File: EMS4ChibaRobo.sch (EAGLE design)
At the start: 31 parts, among them CON1 XT60PB-F, CON2 XT60PB-M, CON3 XT60PB-M, Q2 BUZ11BH, U1 V23134J1052D642, U10 MC34063AD, U4 TLP184, U9 XC6206

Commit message: 大幅な設計変更
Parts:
- removed C22: 47u, rcl:CPOL-EUE2.5-5
- removed C5, C7: 100n, rcl:C-EUC0603
- removed C6: 100p, rcl:C-EUC0603
- removed D3: PMEG6010CEJ,115, nexperia:PMEG6010CEJ,115
- removed L1: L5852, inductors:L5852
- removed R11: 0.68, rcl:R-EU_R1206
- removed R18: 3.6k, rcl:R-EU_R0603
- removed R19: 1.2k, rcl:R-EU_R0603
- removed R28, R30: 1k, rcl:R-EU_R0603
- removed U10: MC34063AD, mc34063:MC34063AD
- removed U4: TLP184, md201x:TLP184
- added C1: 22u, rcl:CPOL-EUE2.5-5
- added C2: 100n, rcl:C-EUC0603
- added IC1: 7805DT, linear:7805DT
- added U$3, U$4: XH-2-STRAIGHT, con-xh:XH-2-STRAIGHT
- renumbered Q2 to Q1
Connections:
- removed net N$1: R11.2, U10.DC, U10.IS, U10.SWC
- removed net N$26: D3.C, L1.1, U10.SWE
- removed net N$27: C6.1, U10.TC
- removed net N$28: R18.1, R19.2, U10.FB
- removed net N$30: R28.1, U4.AC1
- removed net SEND_EMS: U$1.2, U$2.1
- new net LOG_OUT: F1.1, U$3.2, U$4.2
- net !EMS: now also U$1.1; no longer R30.2, U4.E
- net !EMS_ISO: no longer R28.2
- net +12V: now also C1.+, IC1.VI; no longer C7.1, R11.1, U10.VCC
- net +3V3: now also U$1.2; no longer U4.C
- net +5V: now also C2.1, IC1.VO; no longer C22.+, C5.1, L1.2, R18.2, U$1.1
- net BATT_POWER: no longer F1.1
- net GNDIO: now also C1.-, C2.2, IC1.GND, U$2.1, U$3.1, U$4.1; no longer C22.-, C5.2, C6.2, C7.2, D3.A, R19.1, R30.1, U10.GND, U4.AC2
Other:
- moved on the sheet: C19, C20, U9

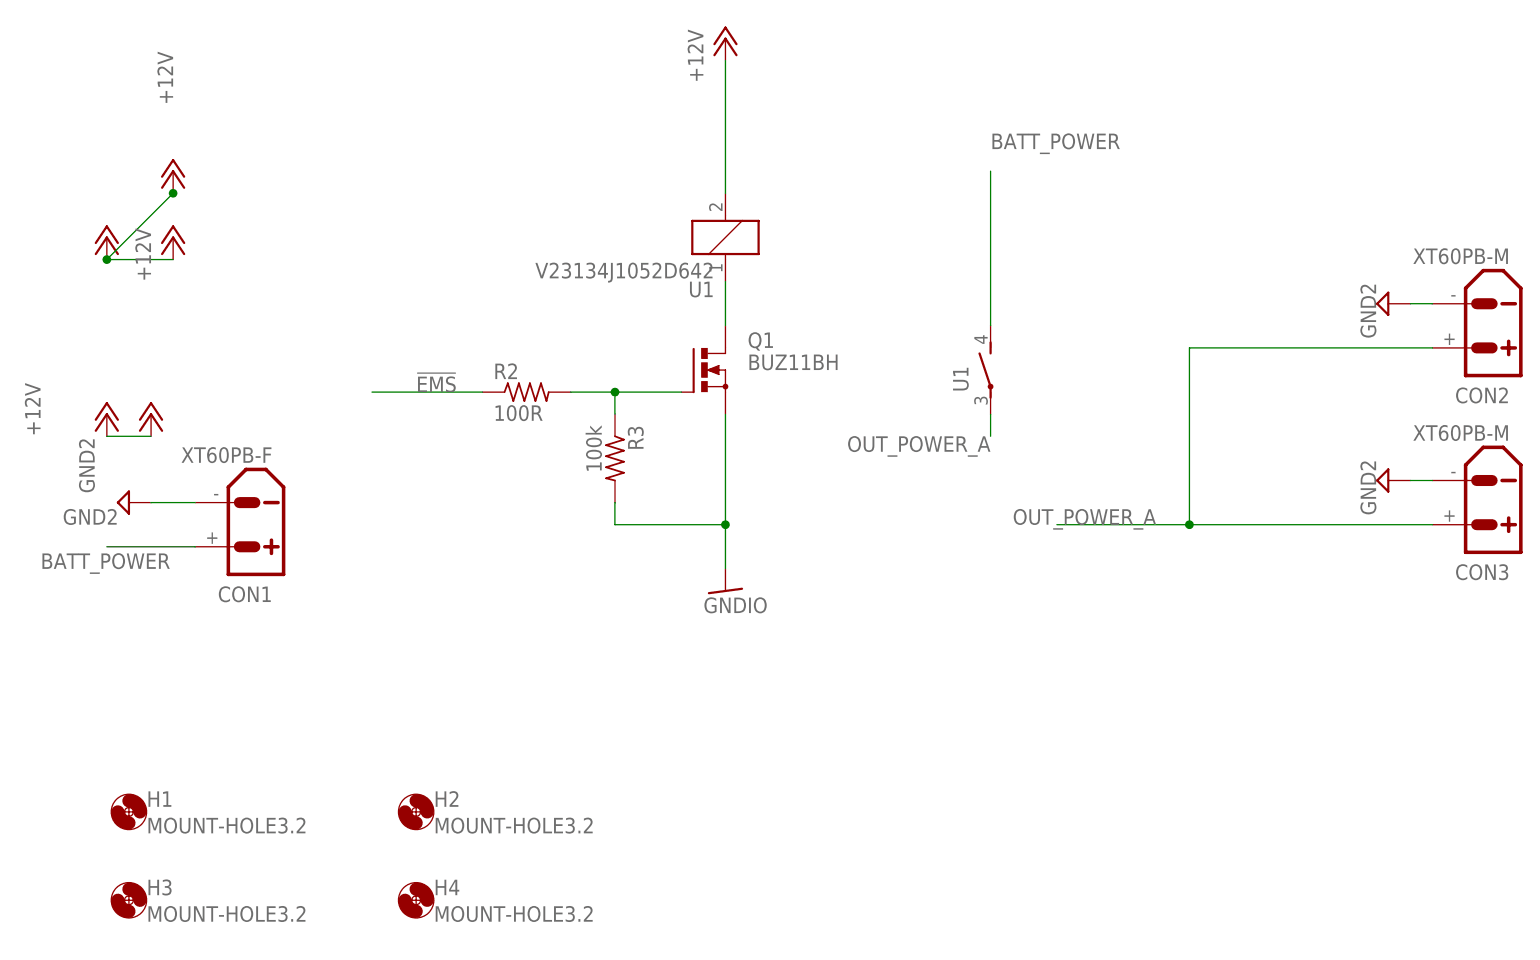
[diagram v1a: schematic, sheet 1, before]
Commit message: relayのフットプリントの改善
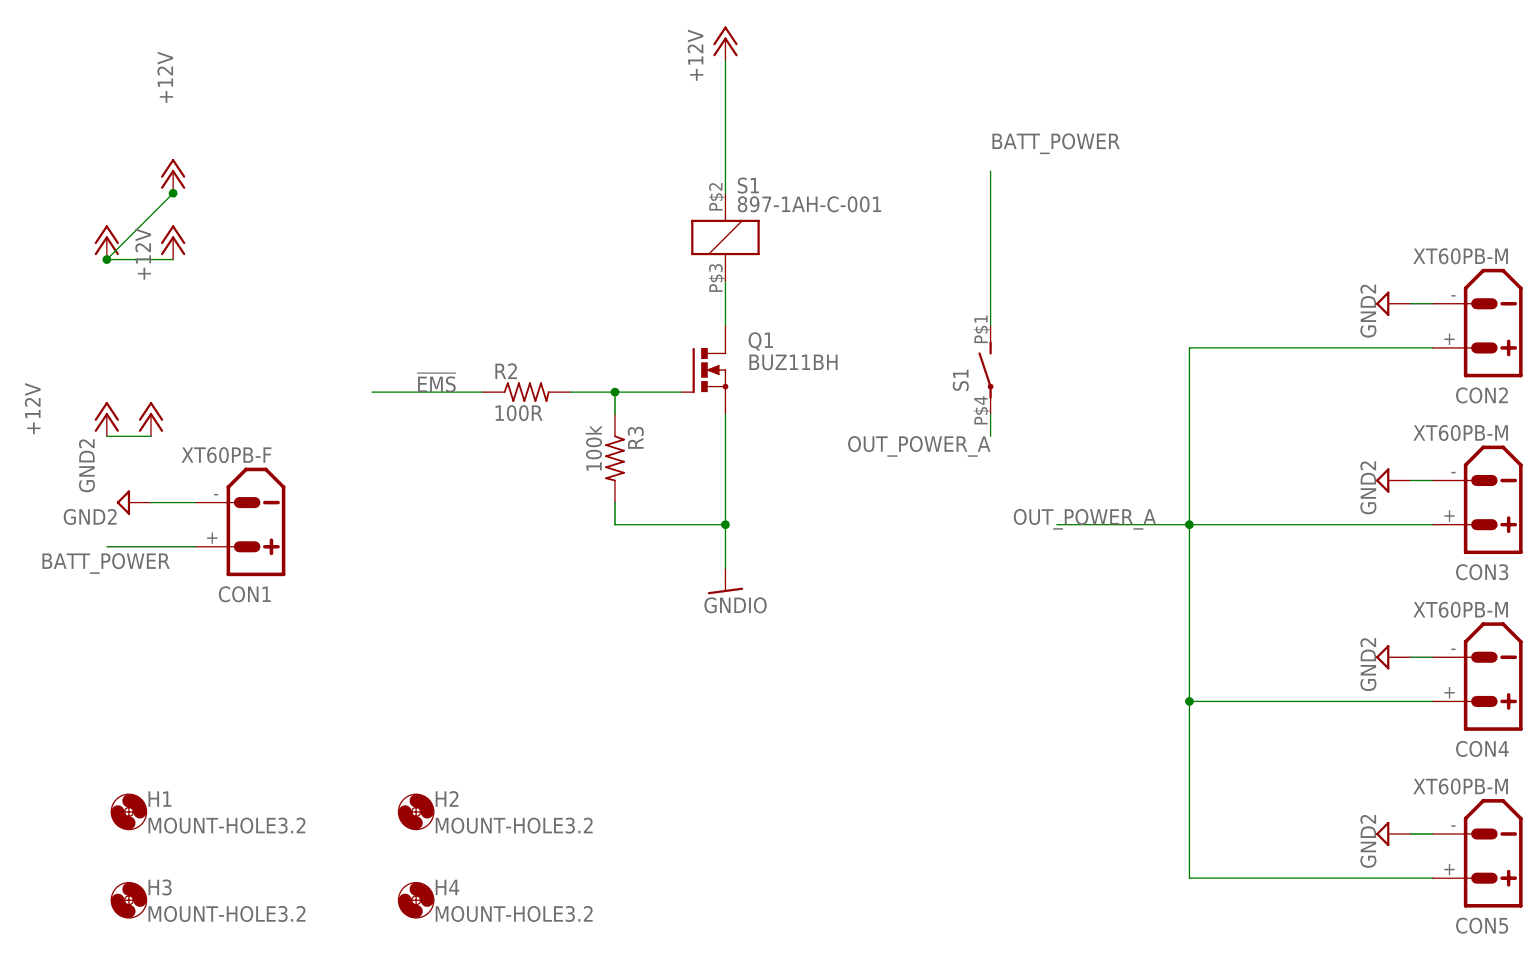
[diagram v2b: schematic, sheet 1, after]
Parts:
- removed U1: V23134J1052D642, relay:V23134J1052D642
- added CON4, CON5: XT60PB-M, amass:XT60PB-M
- added S1: 897-1AH-C-001, relay:897-1AH-C-001
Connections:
- removed net !EMS_ISO: U$2.2
- removed net N$6: Q1.D, U1A.1
- new net N$1: Q1.D, S1U1.2
- net !EMS: now also U$2.2
- net +12V: now also S1U1.1; no longer U1A.2
- net BATT_POWER: now also S1U2.S; no longer U1B.S
- net GND2: now also CON4.-, CON5.-
- net OUT_POWER_A: now also CON4.+, CON5.+, S1U2.P; no longer U1B.P
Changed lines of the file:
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@@
 <part name="SUPPLY7" library="supply2" library_urn="urn:adsk.eagle:library:372" deviceset="GND2" device=""/>
 <part name="SUPPLY8" library="supply2" library_urn="urn:adsk.eagle:library:372" deviceset="GND2" device=""/>
-<part name="U1" library="relay" deviceset="V23134J1052D642" device=""/>
 <part name="H1" library="holes" library_urn="urn:adsk.eagle:library:237" deviceset="MOUNT-HOLE" device="3.2" package3d_urn="urn:adsk.eagle:package:14275/1"/>
 <part name="H2" library="holes" library_urn="urn:adsk.eagle:library:237" deviceset="MOUNT-HOLE" device="3.2" package3d_urn="urn:adsk.eagle:package:14275/1"/>
@@
 <part name="C1" library="rcl" library_urn="urn:adsk.eagle:library:334" deviceset="CPOL-EU" device="E2.5-5" package3d_urn="urn:adsk.eagle:package:23344/1" value="22u"/>
 <part name="C2" library="rcl" library_urn="urn:adsk.eagle:library:334" deviceset="C-EU" device="C0603" package3d_urn="urn:adsk.eagle:package:23616/2" value="100n"/>
+<part name="SUPPLY2" library="supply2" library_urn="urn:adsk.eagle:library:372" deviceset="GND2" device=""/>
+<part name="SUPPLY3" library="supply2" library_urn="urn:adsk.eagle:library:372" deviceset="GND2" device=""/>
+<part name="CON4" library="amass" deviceset="XT60" device="PB-M"/>
+<part name="CON5" library="amass" deviceset="XT60" device="PB-M"/>
+<part name="S1" library="relay" deviceset="897-1AH-C-001" device=""/>
 </parts>
 <sheets>
@@
 <attribute name="VALUE" x="146.685" y="58.293" size="1.778" layer="96" rot="R270"/>
 </instance>
-<instance part="U1" gate="A" x="73.66" y="83.82" smashed="yes" rot="R180">
-<attribute name="VALUE" x="72.39" y="80.899" size="1.778" layer="96" rot="R180"/>
-<attribute name="PART" x="72.39" y="78.74" size="1.778" layer="95" rot="R180"/>
-</instance>
-<instance part="U1" gate="B" x="104.14" y="68.58" smashed="yes">
-<attribute name="PART" x="101.6" y="66.04" size="1.778" layer="95" rot="R90"/>
-</instance>
 <instance part="H1" gate="G$1" x="5.08" y="17.78" smashed="yes">
 <attribute name="NAME" x="7.112" y="18.3642" size="1.778" layer="95"/>
@@
 <attribute name="NAME" x="76.2" y="71.12" size="1.778" layer="95"/>
 <attribute name="VALUE" x="76.2" y="68.58" size="1.778" layer="96"/>
+</instance>
+<instance part="SUPPLY2" gate="G$1" x="149.86" y="15.24" smashed="yes" rot="R270">
+<attribute name="VALUE" x="146.685" y="17.653" size="1.778" layer="96" rot="R270"/>
+</instance>
+<instance part="SUPPLY3" gate="G$1" x="149.86" y="35.56" smashed="yes" rot="R270">
+<attribute name="VALUE" x="146.685" y="37.973" size="1.778" layer="96" rot="R270"/>
+</instance>
+<instance part="CON4" gate="G$1" x="160.02" y="33.02" smashed="yes" rot="R180">
+<attribute name="VALUE" x="163.83" y="41.91" size="1.778" layer="96" rot="R180"/>
+<attribute name="NAME" x="163.83" y="25.908" size="1.778" layer="95" rot="R180"/>
+</instance>
+<instance part="CON5" gate="G$1" x="160.02" y="12.7" smashed="yes" rot="R180">
+<attribute name="VALUE" x="163.83" y="21.59" size="1.778" layer="96" rot="R180"/>
+<attribute name="NAME" x="163.83" y="5.588" size="1.778" layer="95" rot="R180"/>
+</instance>
+<instance part="S1" gate="U1" x="73.66" y="83.82" smashed="yes">
+<attribute name="VALUE" x="74.93" y="86.741" size="1.778" layer="96"/>
+<attribute name="PART" x="74.93" y="88.9" size="1.778" layer="95"/>
+</instance>
+<instance part="S1" gate="U2" x="104.14" y="68.58" smashed="yes">
+<attribute name="PART" x="101.6" y="66.04" size="1.778" layer="95" rot="R90"/>
 </instance>
 </instances>
@@
 <wire x1="154.94" y1="55.88" x2="152.4" y2="55.88" width="0.1524" layer="91"/>
 </segment>
+<segment>
+<pinref part="CON4" gate="G$1" pin="-"/>
+<pinref part="SUPPLY3" gate="G$1" pin="GND2"/>
+<wire x1="154.94" y1="35.56" x2="152.4" y2="35.56" width="0.1524" layer="91"/>
+</segment>
+<segment>
+<pinref part="CON5" gate="G$1" pin="-"/>
+<pinref part="SUPPLY2" gate="G$1" pin="GND2"/>
+<wire x1="154.94" y1="15.24" x2="152.4" y2="15.24" width="0.1524" layer="91"/>
+</segment>
 </net>
 <net name="BATT_POWER" class="0">
 <segment>
 <label x="104.14" y="93.98" size="1.778" layer="95"/>
-<pinref part="U1" gate="B" pin="S"/>
 <wire x1="104.14" y1="73.66" x2="104.14" y2="91.44" width="0.1524" layer="91"/>
+<pinref part="S1" gate="U2" pin="S"/>
 </segment>
 <segment>
@@
 </segment>
 </net>
-<net name="N$6" class="0">
-<segment>
-<pinref part="U1" gate="A" pin="1"/>
-<wire x1="73.66" y1="78.74" x2="73.66" y2="73.66" width="0.1524" layer="91"/>
-<pinref part="Q1" gate="1" pin="D"/>
-</segment>
-</net>
 <net name="OUT_POWER_A" class="0">
 <segment>
+<label x="104.14" y="60.96" size="1.778" layer="95" rot="R180"/>
+<wire x1="104.14" y1="63.5" x2="104.14" y2="60.96" width="0.1524" layer="91"/>
+<pinref part="S1" gate="U2" pin="P"/>
+</segment>
+<segment>
+<wire x1="154.94" y1="30.48" x2="127" y2="30.48" width="0.1524" layer="91"/>
+<wire x1="127" y1="30.48" x2="127" y2="10.16" width="0.1524" layer="91"/>
+<wire x1="127" y1="10.16" x2="154.94" y2="10.16" width="0.1524" layer="91"/>
+<pinref part="CON4" gate="G$1" pin="+"/>
+<pinref part="CON5" gate="G$1" pin="+"/>
 <wire x1="154.94" y1="71.12" x2="127" y2="71.12" width="0.1524" layer="91"/>
 <wire x1="127" y1="71.12" x2="127" y2="50.8" width="0.1524" layer="91"/>
@@
 <pinref part="CON2" gate="G$1" pin="+"/>
 <pinref part="CON3" gate="G$1" pin="+"/>
-</segment>
-<segment>
-<label x="104.14" y="60.96" size="1.778" layer="95" rot="R180"/>
-<pinref part="U1" gate="B" pin="P"/>
-<wire x1="104.14" y1="63.5" x2="104.14" y2="60.96" width="0.1524" layer="91"/>
+<wire x1="127" y1="30.48" x2="127" y2="50.8" width="0.1524" layer="91"/>
+<junction x="127" y="30.48"/>
 </segment>
 </net>
 <net name="+12V" class="1">
-<segment>
-<pinref part="U1" gate="A" pin="2"/>
-<pinref part="P+2" gate="1" pin="+12V"/>
-<wire x1="73.66" y1="88.9" x2="73.66" y2="104.14" width="0.1524" layer="91"/>
-</segment>
 <segment>
 <pinref part="P+4" gate="1" pin="+12V"/>
@@
 <pinref part="P+10" gate="1" pin="+12V"/>
 <wire x1="7.62" y1="60.96" x2="2.54" y2="60.96" width="0.1524" layer="91"/>
+</segment>
+<segment>
+<pinref part="P+2" gate="1" pin="+12V"/>
+<wire x1="73.66" y1="104.14" x2="73.66" y2="88.9" width="0.1524" layer="91"/>
+<pinref part="S1" gate="U1" pin="1"/>
+</segment>
+</net>
+<net name="N$1" class="0">
+<segment>
+<pinref part="Q1" gate="1" pin="D"/>
+<wire x1="73.66" y1="78.74" x2="73.66" y2="73.66" width="0.1524" layer="91"/>
+<pinref part="S1" gate="U1" pin="2"/>
 </segment>
 </net>
@@
 <label x="93.98" y="93.98" size="1.778" layer="95"/>
 </segment>
+<segment>
+<pinref part="U$2" gate="G$1" pin="2"/>
+<wire x1="88.9" y1="76.2" x2="93.98" y2="76.2" width="0.1524" layer="91"/>
+<label x="93.98" y="76.2" size="1.778" layer="95"/>
+</segment>
 </net>
 <net name="+12V" class="1">
@@
 <wire x1="-25.4" y1="144.78" x2="-33.02" y2="144.78" width="0.1524" layer="91"/>
 <label x="-33.02" y="144.78" size="1.778" layer="95"/>
-</segment>
-</net>
-<net name="!EMS_ISO" class="0">
-<segment>
-<pinref part="U$2" gate="G$1" pin="2"/>
-<wire x1="88.9" y1="76.2" x2="93.98" y2="76.2" width="0.1524" layer="91"/>
-<label x="93.98" y="76.2" size="1.778" layer="95"/>
 </segment>
 </net>
@@
 packages will not be understood (or retained) with this version.
 </note>
+<note version="8.4" severity="warning">
+Since Version 8.4, EAGLE supports properties for SPICE simulation.
+Probes in schematics and SPICE mapping objects found in parts and library devices
+will not be understood with this version. Update EAGLE to the latest version
+for full support of SPICE simulation.
+</note>
 </compatibility>
